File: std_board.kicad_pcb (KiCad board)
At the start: 2 copper layers, 99.1 x 99.1 mm, 192 parts, among them IC1 ESP32, IC2 ACS712, IC3 L78L05, IC4 AMS1117-V, J1 Jumper, J10 J_DHT11, J11 Jumper, J12 Jumper, J14 Jumper, J15 Jumper, J16 J_PRess, J17 Jumper, J18 Jumper, J19 Jumper, J2 Jumper, J20 Jumper, J21 Jumper, J22 Jumper, J23 Jumper, J24 Jumper, J25 Jumper, J26 Jumper, J3 Jumper, J31 Jumper, J32 Jumper, J33 Jumper, J34 Jumper, J35 Jumper, J36 Jumper, J37 Jumper, J38 Jumper, J39 Jumper, J4 Jumper, J40 Jumper, J41 Jumper, J42 Jumper, J43 Jumper, J44 Jumper, J45 Jumper, J5 Jumper, J7 Jumper, J8 Jumper, J9 Jumper, T1 TRIAC_Micro, T2 TRIAC_Micro, T3 TRIAC_Micro, T4 NPN_MMBT222A, T5 NPN_MMBT222A, T6 NPN_MMBT222A, T7 NPN_MMBT222A, T8 PNP_2N3906, T9 NPN_MMBT222A, U1 LNK306

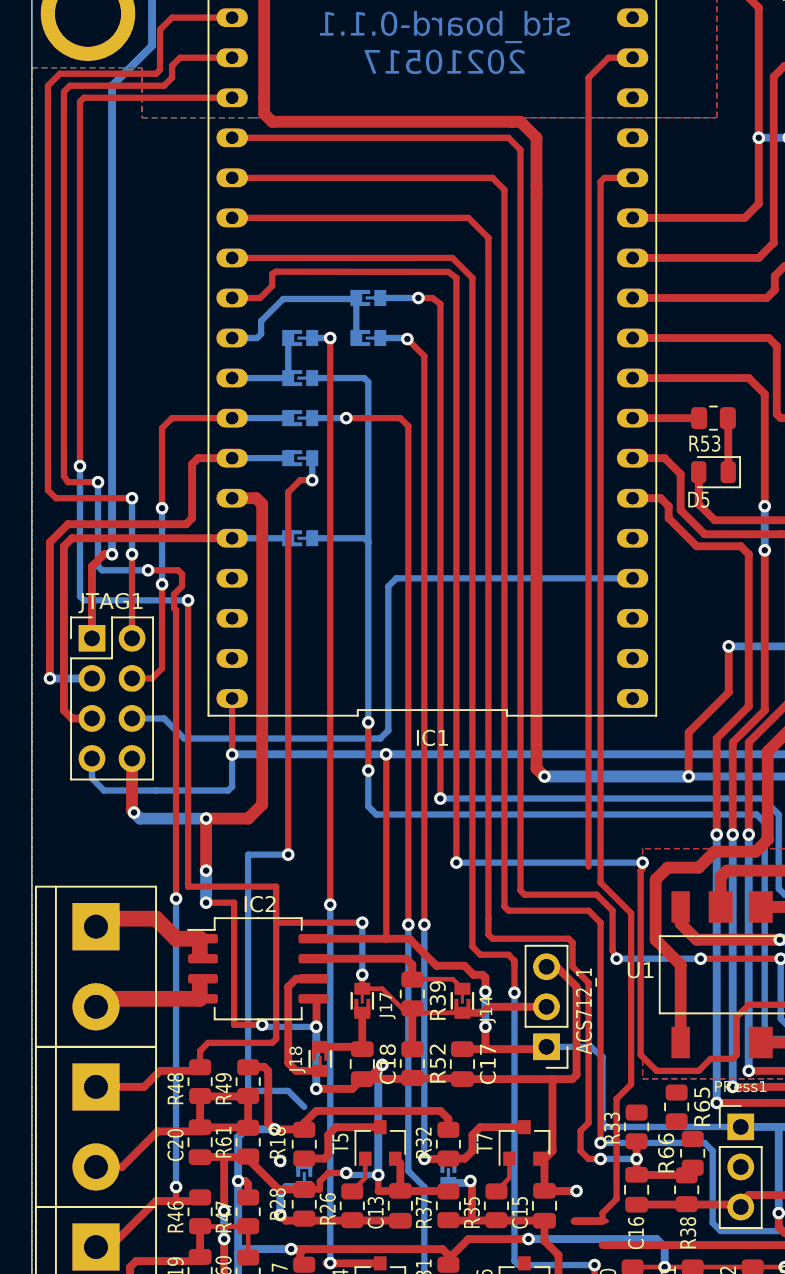
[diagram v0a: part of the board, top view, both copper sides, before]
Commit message: recalculated current sensor resistors and changed pins and jumps of levels and sensors
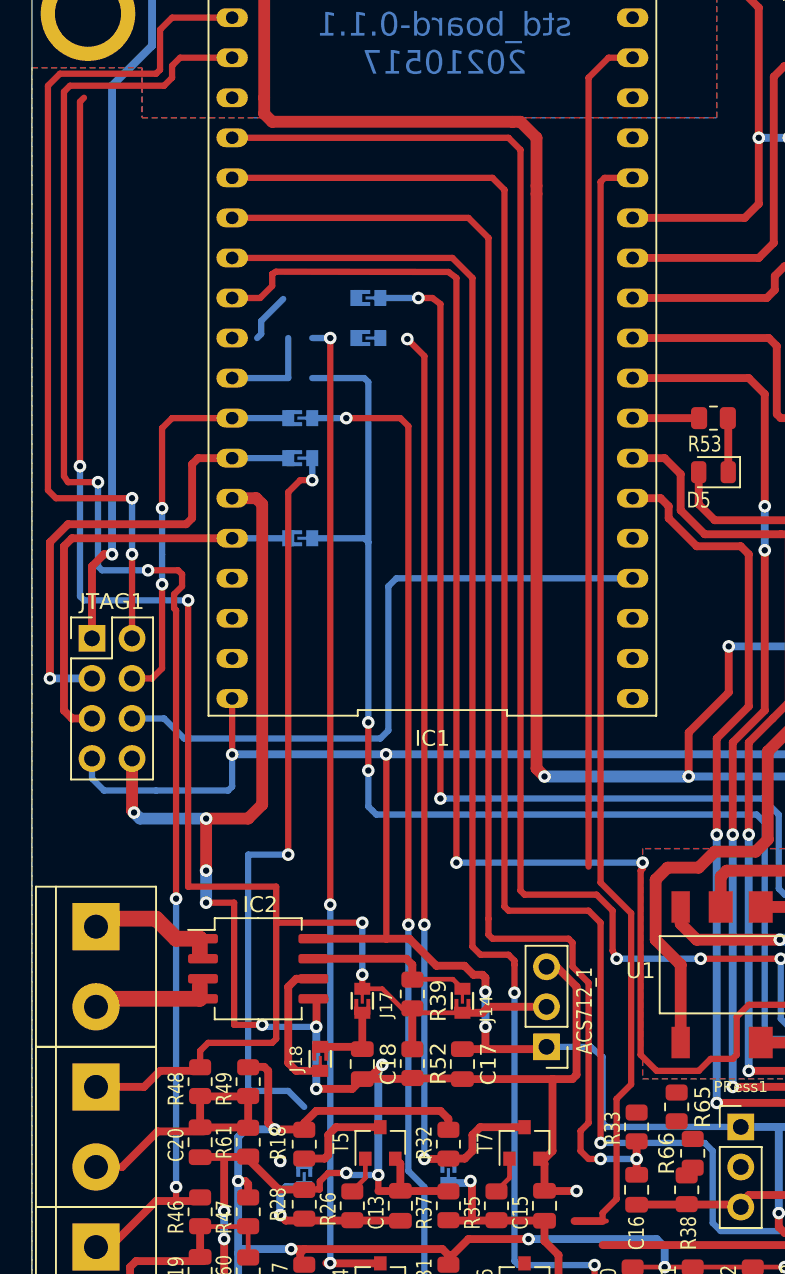
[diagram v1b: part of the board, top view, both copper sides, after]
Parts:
- removed J7, J8: Jumper, thmalmeida:J_0603
- R42: value 680 k -> 1 M
- R45: value 220 k -> 180 k
- R46, R48: value 3.3 k -> 120
- R47, R49: value 3.3 k -> 180 k
- R59: value 220 k -> 120 k
- R60, R61: value 3.3 k -> 120 k
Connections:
- IC1 pad 10: P10 -> /L1_in
- IC1 pad 11: P11 -> /L2_in
- IC1 pad 4: /iSensor2 -> P03
- J22 pad 1: P10 -> P03
- J22 pad 2: /L4_in -> /iSensor2
- J24 pad 1: P10 -> P03
- J26 pad 2: /L2_in -> /L4_in
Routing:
- net /L4_in: track 62.2 -> 108.2 mm, vias 3 -> 5
- net /L2_in: track 54.0 -> 12.5 mm, vias 2 -> 0
- net P10: track 12.8 -> 3.16 mm
- net /iSensor2: track 126.1 -> 116.7 mm
- net P11: track 6.10 -> 0.00 mm
- net /PRess_1: track 89.7 -> 86.4 mm

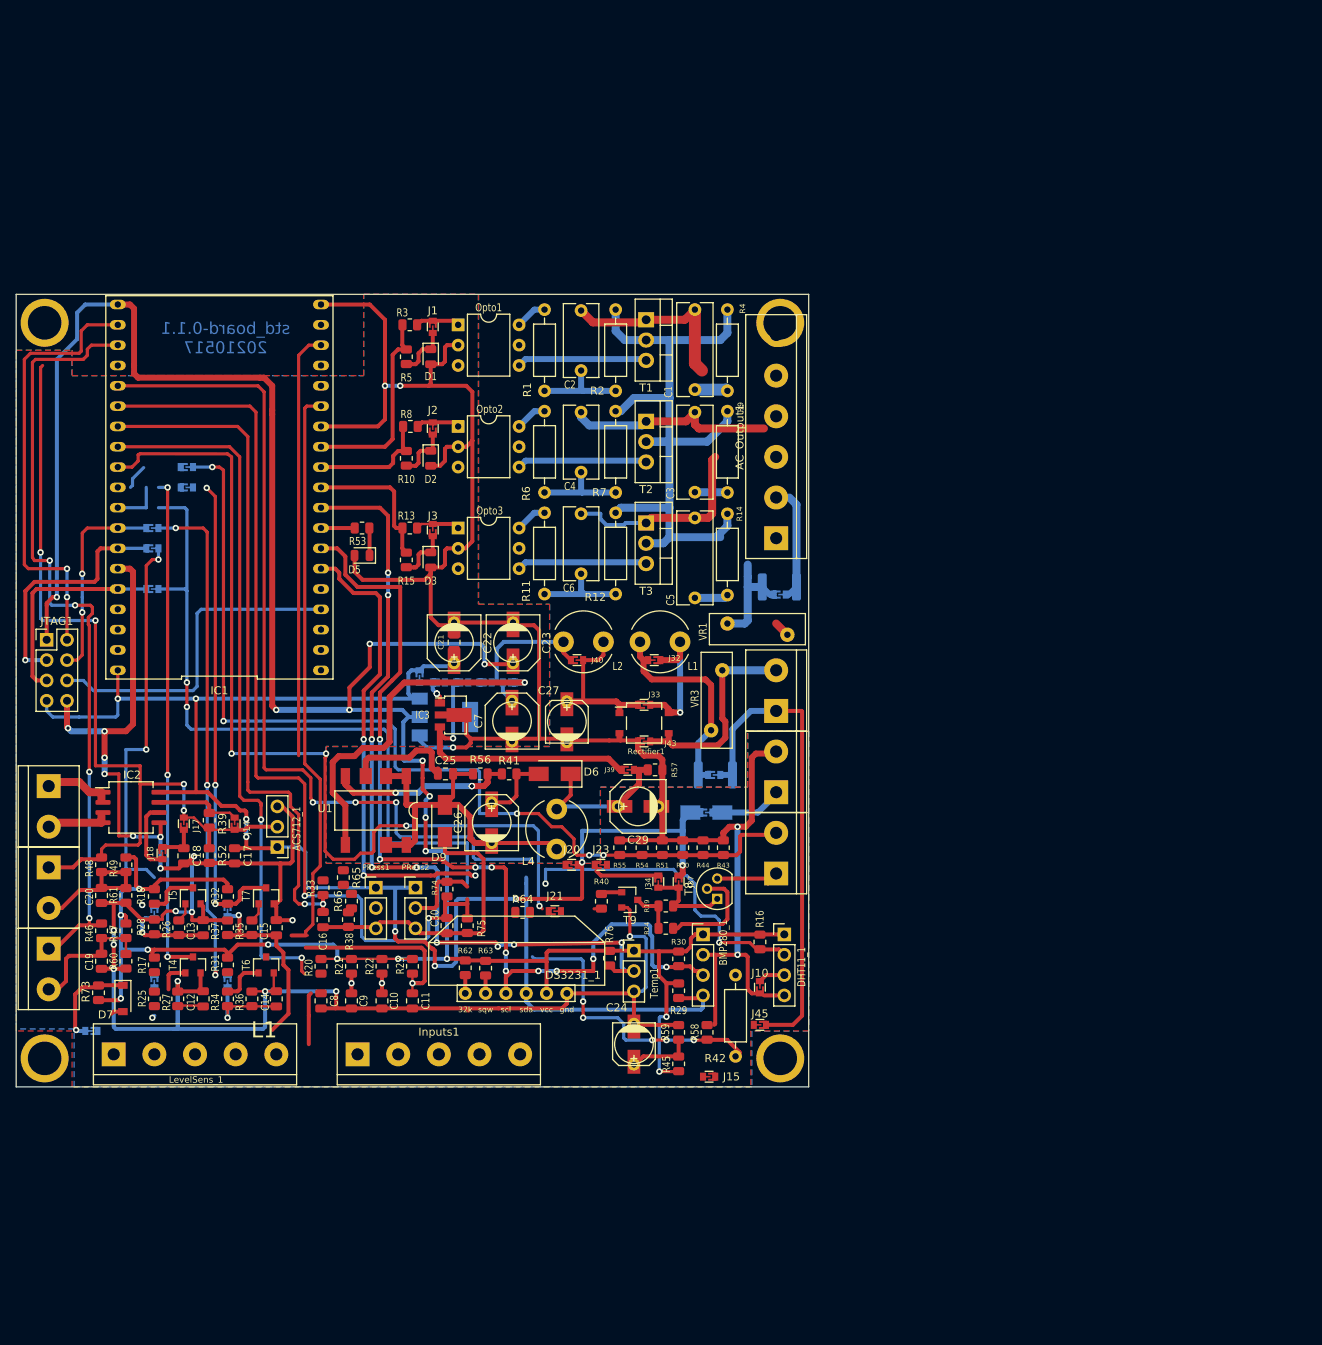
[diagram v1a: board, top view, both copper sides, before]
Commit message: added new triac circuit upgrade to soft starter
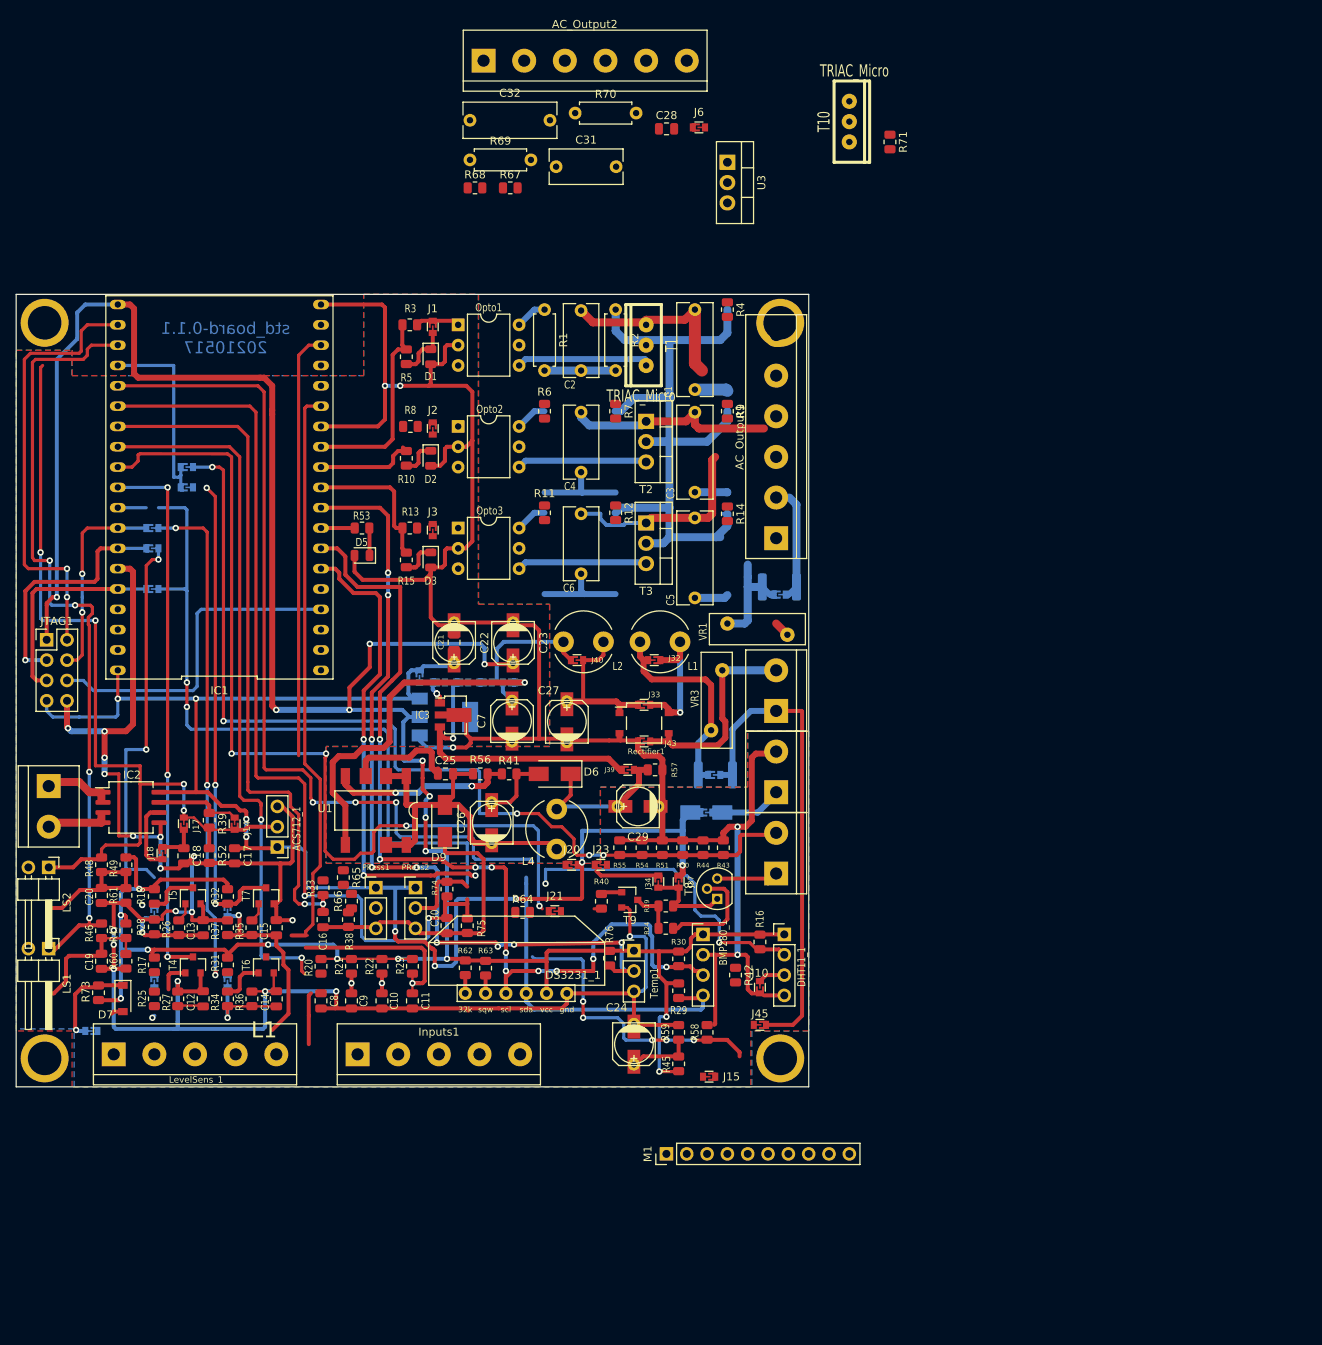
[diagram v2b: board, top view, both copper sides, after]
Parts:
- added AC_Output2: Driver_AC_1, TerminalBlock:TerminalBlock_bornier-6_P5.08mm, F.Cu at (58.4, -30.5)
- added C28: 1 uF, Capacitor_SMD:C_0805_2012Metric, F.Cu at (81.3, -22.0)
- added C31: 47 nF, Capacitor_THT:C_Rect_L9.0mm_W4.2mm_P7.50mm_MKT, F.Cu at (67.5, -17.2)
- added C32: 10 nF, Capacitor_THT:C_Rect_L11.5mm_W4.3mm_P10.00mm_MKT, F.Cu at (56.7, -23.0)
- added J6: Jumper, thmalmeida:J_0603, F.Cu at (85.3, -22.1)
- added M1: ADS1x15_module, Connector_PinHeader_2.54mm:PinHeader_1x10_P2.54mm_Vertical, F.Cu at (81.3, 106.2)
- added R67: 680, Resistor_SMD:R_0805_2012Metric, F.Cu at (61.8, -14.6)
- added R68: 1 k, Resistor_SMD:R_0805_2012Metric, F.Cu at (57.4, -14.6)
- added R69: 330, Resistor_THT:R_Axial_DIN0207_L6.3mm_D2.5mm_P7.62mm_Horizontal, F.Cu at (56.7, -18.1)
- added R70: 470, Resistor_THT:R_Axial_DIN0207_L6.3mm_D2.5mm_P7.62mm_Horizontal, F.Cu at (69.9, -23.9)
- added R71: 39, Resistor_SMD:R_0805_2012Metric, F.Cu at (109.2, -20.3)
- added T10: TRIAC_Micro, thmalmeida:TO-220_thm, F.Cu at (104.1, -22.9)
- added U3: L7805CV, Package_TO_SOT_THT:TO-220-3_Vertical, F.Cu at (88.9, -17.8)
- C22, C23, C26, C29, C7: footprint thmalmeida:C4_elec_7x6.7_pth -> thmalmeida:C3_elec_5x4.5_pth
- LS1, LS2: footprint TerminalBlock:TerminalBlock_bornier-2_P5.08mm -> Connector_PinHeader_2.54mm:PinHeader_1x02_P2.54mm_Horizontal
- R1, R2: footprint Resistor_THT:R_Axial_DIN0207_L6.3mm_D2.5mm_P10.16mm_Horizontal -> Resistor_THT:R_Axial_DIN0207_L6.3mm_D2.5mm_P7.62mm_Horizontal
- R10, R15: value R_Micro -> 1 k
- R11, R12, R14, R4, R42, R6, R7, R9: footprint Resistor_THT:R_Axial_DIN0207_L6.3mm_D2.5mm_P10.16mm_Horizontal -> Resistor_SMD:R_0805_2012Metric
- R13, R8: value R_Micro -> 680
- R3: value 470 -> 680
- R5: value 470 -> 1 k
- T1: footprint Package_TO_SOT_THT:TO-220-3_Vertical -> thmalmeida:TO-220_thm
- moved T1 3.17 mm to (78.7, 5.08), turned to 180 degrees
- turned J2 to -90 degrees
- turned J3 to -90 degrees
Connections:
- AC_Output1 pad 4: /Power_AC -> /Load00
- IC1 pad 16: (no net) -> unconnected-(IC1-Pad16)
- IC1 pad 17: (no net) -> unconnected-(IC1-Pad17)
- IC1 pad 18: (no net) -> unconnected-(IC1-Pad18)
- IC1 pad 20: (no net) -> unconnected-(IC1-Pad20)
- IC1 pad 21: (no net) -> unconnected-(IC1-Pad21)
- IC1 pad 22: (no net) -> unconnected-(IC1-Pad22)
- IC1 pad 24: (no net) -> unconnected-(IC1-Pad24)
- IC1 pad 34: (no net) -> unconnected-(IC1-Pad34)
- IC1 pad 35: (no net) -> unconnected-(IC1-Pad35)
- IC1 pad 6: /PRess_2 -> /PRess_1
- IC1 pad 7: /PRess_1 -> /PRess_2
- J15 pad 1: /Power_AC_2 -> /Power_AC_R_2
- J2 pad 1: Net-(D2-Pad1) -> Net-(J2-Pad1)
- J2 pad 2: Net-(J2-Pad2) -> Net-(D2-Pad1)
- J3 pad 1: Net-(D3-Pad1) -> Net-(J3-Pad1)
- J3 pad 2: Net-(J3-Pad2) -> Net-(D3-Pad1)
- J35 pad 2: Net-(IC3-Pad1) -> Net-(J35-Pad2)
- J36 pad 1: /Power_AC_2 -> /Power_AC_R_2
- J36 pad 2: /Power_AC -> /Power_AC_R
- J42 pad 1: Net-(IC3-Pad1) -> Net-(J35-Pad2)
- Opto2 pad 1: Net-(J2-Pad2) -> Net-(J2-Pad1)
- Opto3 pad 1: Net-(J3-Pad2) -> Net-(J3-Pad1)
- R12 pad 1: /Power_AC_2 -> /Power_AC_T
- R13 pad 2: Net-(J3-Pad2) -> Net-(J3-Pad1)
- R14 pad 1: /Power_AC_2 -> /Power_AC_T
- R2 pad 1: /Power_AC_2 -> /Power_AC_R
- R4 pad 1: /Power_AC_2 -> /Power_AC_R
- R7 pad 1: /Power_AC_2 -> /Power_AC_S
- R8 pad 1: /K2_out -> Net-(J2-Pad1)
- R8 pad 2: Net-(J2-Pad2) -> /K2_out
- R9 pad 1: /Power_AC_2 -> /Power_AC_S
- T1 pad 2: /Power_AC_2 -> /Power_AC_R
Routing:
- net P03: track 0.00 -> 24.5 mm
- net /Power_AC_2: track 102.9 -> 89.6 mm
- net /Power_AC_R_2: track 0.00 -> 13.3 mm
- net /Power_AC_R: track 0.00 -> 13.3 mm
- net /Power_AC: track 13.3 -> 0.00 mm
- net Net-(J3-Pad2): track 5.53 -> 0.00 mm
- net Net-(J2-Pad2): track 5.45 -> 0.00 mm
- net /L1_in: track 63.3 -> 68.3 mm
- net Net-(J35-Pad2): track 0.00 -> 4.58 mm, vias 0 -> 2
- net Net-(IC3-Pad1): track 4.58 -> 0.00 mm, vias 2 -> 0
- net P10: track 3.16 -> 0.00 mm
- net Net-(C2-Pad1): track 11.5 -> 8.89 mm
- net /K2_out: track 15.2 -> 12.6 mm
- net /L2_in: track 12.5 -> 9.95 mm
- net Net-(D3-Pad1): track 6.71 -> 4.93 mm
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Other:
- net class Default removed
- net class Power AC removed
- board text added: "(GPIO19) K3_in"
- board text added: "- Dev_1: JTAG connector; - Dev_2: ACS712 current sensor; - Dev_3: Pressure sensor 1 (GPIO32 or ADC1_4); - Dev_4: Pressure sensor 2 (GPIO35 or ADC1_7); - Dev_5: DS3231 RTC; - Dev_6: DS18B20, 1 wire temp. sensor; - Dev_7: BMP150, pressure sensor; - Dev_8: DHT11 humidity sensor; - Dev_9: Voltage Measure (GPIO34)."
- board text added: "CT Coil A1 (GPIO36)"
- board text removed: "(GPIO21) K3_in"
- board text removed: "- Dev_1: JTAG connector; - Dev_2: ACS712 current sensor; - Dev_3: Pressure sensor 1; - Dev_4: Pressure sensor 2; - Dev_5: DS3231 RTC; - Dev_6: DS18B20, 1 wire temp. sensor; - Dev_7: BMP150, pressure sensor; - Dev_8: DHT11 humidity sensor."
- board text removed: "CT Coil A1"

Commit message: board update some documentation of pinout link with description
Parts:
- removed AC_Output2: Driver_AC_1, TerminalBlock:TerminalBlock_bornier-6_P5.08mm
- removed C28: 1 uF, Capacitor_SMD:C_0805_2012Metric
- removed C31: 47 nF, Capacitor_THT:C_Rect_L9.0mm_W4.2mm_P7.50mm_MKT
- removed C32: 10 nF, Capacitor_THT:C_Rect_L11.5mm_W4.3mm_P10.00mm_MKT
- removed IC3: L78L05, Package_TO_SOT_SMD:SOT-89-3
- removed J6: Jumper, thmalmeida:J_0603
- removed R11, R6: 360, Resistor_SMD:R_0805_2012Metric
- removed R12, R7: 470, Resistor_SMD:R_0805_2012Metric
- removed R14, R9: 47, Resistor_SMD:R_0805_2012Metric
- removed R4, R71: 39, Resistor_SMD:R_0805_2012Metric
- removed R67: 680, Resistor_SMD:R_0805_2012Metric
- removed R68: 1 k, Resistor_SMD:R_0805_2012Metric
- removed R69: 330, Resistor_THT:R_Axial_DIN0207_L6.3mm_D2.5mm_P7.62mm_Horizontal
- removed R70: 470, Resistor_THT:R_Axial_DIN0207_L6.3mm_D2.5mm_P7.62mm_Horizontal
- removed T10: TRIAC_Micro, thmalmeida:TO-220_thm
- R45: value 180 k -> 39 k
- R46, R48: value 120 -> 3.3 k
- R47: value 180 k -> 56 k
- R60: value 120 k -> 39 k
- moved U3 102.8 mm to (121.6, 79.7)
- moved C7 74.7 mm to (130.5, 81.7)
- moved C27 74.3 mm to (137.0, 81.7)
- moved J33 73.4 mm to (144.6, 81.9), turned to -90 degrees
- moved Rectifier1 71.2 mm to (143.3, 81.7), turned to -90 degrees
- moved J43 69.1 mm to (142.0, 81.9), turned to -90 degrees
- moved C21 69.0 mm to (116.8, 72.4)
- moved C25 69.0 mm to (115.7, 88.9)
- moved D6 69.0 mm to (129.3, 88.9)
- moved J3 69.0 mm to (114.1, 58.4)
- moved 24Vac_In1 69.0 mm to (157.0, 81.0)
- moved ACS712_1 69.0 mm to (94.7, 98.0)
- moved AC_Output1 69.0 mm to (157.0, 59.4)
- moved BMP280_1 69.0 mm to (147.9, 108.9)
- moved C1 69.0 mm to (146.8, 40.8)
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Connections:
- 24Vac_In1 pad 2: Net-(24Vac_In1-Pad2) -> Net-(24Vac_In1-S2)
- J1 pad 1: Net-(J1-Pad1) -> Net-(J1-A)
- J1 pad 2: Net-(D1-Pad1) -> Net-(D1-+Anode)
- J10 pad 2: Net-(DHT11_1-Pad3) -> Net-(J10-B)
- J14 pad 2: Net-(IC2-Pad7) -> Net-(IC2-VIOUT)
- J18 pad 2: Net-(IC2-Pad6) -> Net-(IC2-Filter)
- J2 pad 1: Net-(J2-Pad1) -> Net-(J2-A)
- J2 pad 2: Net-(D2-Pad1) -> Net-(D2-+Anode)
- J3 pad 1: Net-(J3-Pad1) -> Net-(J3-A)
- J3 pad 2: Net-(D3-Pad1) -> Net-(D3-+Anode)
- J31 pad 1: Net-(F3-Pad1) -> Net-(F3-A)
- J32 pad 2: Net-(F3-Pad1) -> Net-(F3-A)
- J42 pad 1: Net-(J35-Pad2) -> /+5V
- J43 pad 2: Net-(24Vac_In1-Pad2) -> Net-(24Vac_In1-S2)
- L1 pad 2: Net-(F3-Pad1) -> Net-(F3-A)
- R1 pad 1: Net-(Opto1-Pad6) -> Net-(R1-A)
- R10 pad 2: Net-(D2-Pad1) -> Net-(D2-+Anode)
- R13 pad 2: Net-(J3-Pad1) -> Net-(J3-A)
- R15 pad 2: Net-(D3-Pad1) -> Net-(D3-+Anode)
- R19 pad 1: Net-(R19-Pad1) -> Net-(R19-A)
- R24 pad 2: Net-(R19-Pad1) -> Net-(R19-A)
- R25 pad 2: Net-(R25-Pad2) -> Net-(R25-B)
- R26 pad 2: Net-(R26-Pad2) -> Net-(R26-B)
- R3 pad 2: Net-(J1-Pad1) -> Net-(J1-A)
- R34 pad 2: Net-(R34-Pad2) -> Net-(R34-B)
- R35 pad 2: Net-(R35-Pad2) -> Net-(R35-B)
- R39 pad 1: Net-(IC2-Pad7) -> Net-(IC2-VIOUT)
- R40 pad 2: Net-(R40-Pad2) -> Net-(R40-B)
- R5 pad 2: Net-(D1-Pad1) -> Net-(D1-+Anode)
- R53 pad 2: Net-(D5-Pad1) -> Net-(D5-+Anode)
- R8 pad 1: Net-(J2-Pad1) -> Net-(J2-A)
- Rectifier1 pad 3: Net-(24Vac_In1-Pad2) -> Net-(24Vac_In1-S2)
- T1 pad 3: Net-(Opto1-Pad4) -> Net-(T1-G)
- U3 pad 1: Net-(J35-Pad2) -> /+5V
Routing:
- net /Power_AC_2: track 89.6 -> 0.00 mm
- net GND: track 557.0 -> 503.3 mm
- net /C: track 46.0 -> 10.2 mm
- net /+5V: track 189.0 -> 157.6 mm
- net /Load02: track 26.3 -> 0.00 mm
- net /Load03: track 25.2 -> 0.00 mm
- net /Load01: track 24.5 -> 0.00 mm
- net Net-(F3-Pad1): track 27.4 -> 8.10 mm
- net Net-(Opto2-Pad4): track 16.3 -> 0.00 mm
- net Net-(Opto1-Pad4): track 16.3 -> 0.00 mm
- net Net-(Opto3-Pad4): track 16.3 -> 0.00 mm
- net Net-(J33-A): track 19.7 -> 4.45 mm
- net /Power_AC_R_2: track 13.3 -> 0.00 mm
- net Net-(J32-A): track 17.8 -> 4.53 mm, vias 1 -> 0
- net /Power_AC_R: track 13.3 -> 0.00 mm
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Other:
- board text added: "- Dev_1: JTAG connector; - Dev_2: ACS712 current sensor; - Dev_3: Pressure sensor 1 (GPIO32 or ADC1_4); - Dev_4: Pressure sensor 2 (GPIO35 or ADC1_7); - Dev_5: DS3231 RTC (SDA-GPIO00; SCL-GPIO04); - Dev_6: DS18B20, 1 wire temp. sensor (GPIO17); - Dev_7: BMP150, pressure sensor (SDA-GPIO00; SCL-GPIO04);; - Dev_8: DHT11 humidity sensor (GPIO27 or GPIO13); - Dev_9: Voltage Measure (GPIO34)."
- board text added: "CT Coil B1 (GPIO39)"
- board text removed: "- Dev_1: JTAG connector; - Dev_2: ACS712 current sensor; - Dev_3: Pressure sensor 1 (GPIO32 or ADC1_4); - Dev_4: Pressure sensor 2 (GPIO35 or ADC1_7); - Dev_5: DS3231 RTC; - Dev_6: DS18B20, 1 wire temp. sensor; - Dev_7: BMP150, pressure sensor; - Dev_8: DHT11 humidity sensor; - Dev_9: Voltage Measure (GPIO34)."
- board text removed: "CT Coil B1"
